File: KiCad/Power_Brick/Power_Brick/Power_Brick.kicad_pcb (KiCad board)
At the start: 2 copper layers, 70 x 70 mm, 109 parts, among them J1 Conn_01x10, J2 Conn_01x09, J3 MKDS5_2-9_5_1pos_PowerPad, J4 MKDS5_2-9_5_1pos_PowerPad, J5 MKDS5_2-9_5_4pos_PowerPad, J6 Conn_01x04, J7 Conn_01x04, Q1 CSD18540Q5B, Q2 CSD18540Q5B, Q3 CSD18540Q5B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

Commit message: KiCad beta
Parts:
- SW1: footprint PCM_SparkFun-Switch:Push_SMD_5.2x5.2mm_h1.9mm -> PCM_SparkFun-Switch:Push_SMD_4.6x2.8mm_h1.9mm
- moved D1 6.68 mm to (221.6, 126.5), turned to 180 degrees
- moved D2 6.58 mm to (203.0, 126.2), turned to 0 degrees
- moved D3 3.77 mm to (202.8, 132.0), turned to -90 degrees
- moved R1 3.45 mm to (219.6, 126.5)
- moved R2 3.45 mm to (218.4, 126.5)
- moved C1 1.93 mm to (205.0, 125.0)
- moved R3 1.89 mm to (206.0, 125.0)
- moved SW1 1.81 mm to (221.5, 129.0)
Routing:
- net GND: track 39.1 -> 31.3 mm, vias 139 -> 146
- net +3.3V: track 162.3 -> 158.3 mm
- net VBUS: track 36.4 -> 32.6 mm
- net Net-(D2-A): track 1.41 -> 5.19 mm
- net Net-(D1-A): track 3.96 -> 1.53 mm
- net /FAULT_N: track 28.9 -> 26.6 mm
- net +5V: track 12.3 -> 10.1 mm
- net /RESET: track 31.4 -> 30.2 mm

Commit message: KiCad beta
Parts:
- moved C8 31.6 mm to (186.2, 140.8), turned to 0 degrees
- moved NT8 2.00 mm to (190.5, 139.8)
- moved J5 0.59 mm to (212.5, 96.8)
- turned C6 to 0 degrees
- turned C7 to 0 degrees
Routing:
- net VBUS: track 32.6 -> 49.9 mm, vias 88 -> 97
- net GND: track 31.3 -> 24.7 mm, vias 146 -> 129

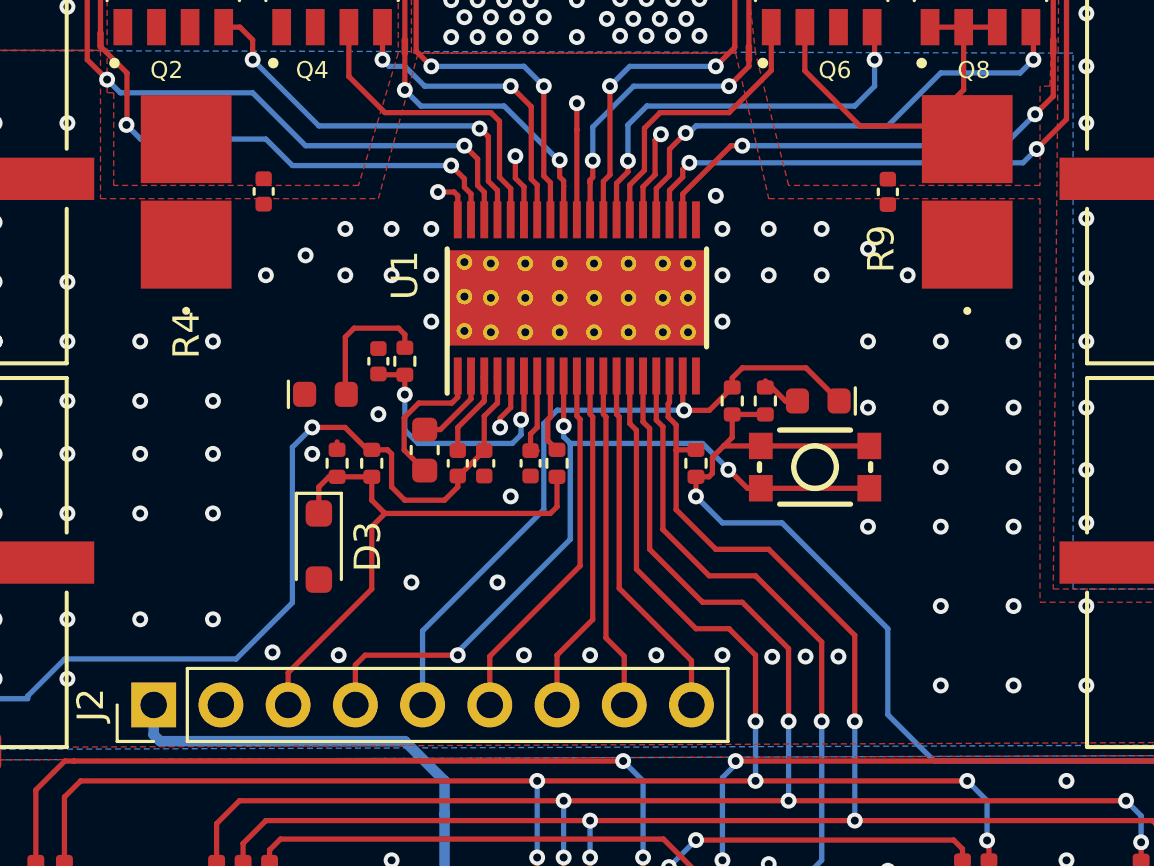
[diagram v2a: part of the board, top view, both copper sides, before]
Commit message: Revised fault and capacitor ratings
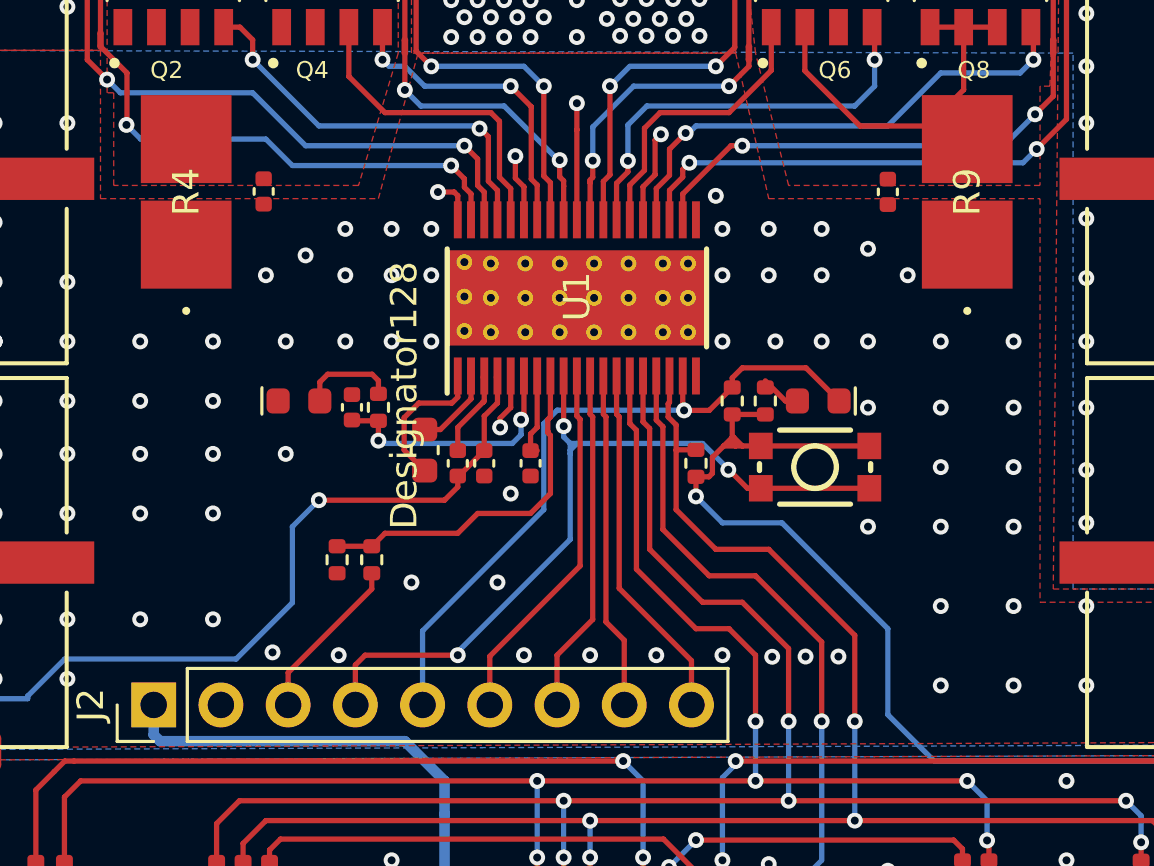
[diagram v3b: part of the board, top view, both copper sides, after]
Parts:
- removed D3: Zener, Diode_SMD:D_SOD-323_HandSoldering
- removed R5: 100k, PCM_SparkFun-Resistor:R_0402_1005Metric
- R7: value 22 -> 330
- moved R7 7.89 mm to (204.8, 132.5), turned to -90 degrees
- moved R6 3.64 mm to (203.4, 132.5), turned to 90 degrees
- moved C1 2.01 mm to (204.0, 126.7)
- moved R3 2.01 mm to (205.0, 126.7)
- moved D2 1.03 mm to (202.0, 126.5)
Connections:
- R6 pad 2: /SLEEP_N_IN -> /SLEEP_N
- R7 pad 1: /SLEEP_N_IN -> /SLEEP_N
- R7 pad 2: /SLEEP_N -> /SLEEP_N_IN
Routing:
- net /SLEEP_N_IN: track 21.2 -> 6.29 mm
- net /SLEEP_N: track 2.98 -> 13.4 mm
- net VBUS: track 49.9 -> 45.2 mm
- net Net-(D2-A): track 5.19 -> 3.65 mm
- net +3.3V: track 158.3 -> 159.2 mm
- net +5V: track 10.1 -> 9.60 mm
- net GND: track 24.7 -> 24.4 mm, vias 129 -> 133

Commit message: DRC, Silkscreen Updates
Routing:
- net GND: vias 133 -> 132
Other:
- board text added: "3.3"
- board text added: "A1"
- board text added: "A2"
- board text added: "B1"
- board text added: "B2"
- board text added: "CS0"
- board text added: "CS1"
- board text added: "CS2"
- board text added: "DR1"
- board text added: "DR2"
- board text added: "FLT"
- board text added: "GND"
- board text added: "RST"
- board text added: "SCL"
- board text added: "SDI"
- board text added: "SDO"
- board text added: "SLP"

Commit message: Digital Grount Updates
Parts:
- moved R6 4.62 mm to (208.0, 131.8)
- moved R7 4.32 mm to (209.0, 131.8)
- moved SW1 2.47 mm to (219.8, 130.8), turned to 90 degrees
- moved D2 1.25 mm to (203.0, 127.2), turned to 90 degrees
- moved D1 0.84 mm to (222.0, 127.2), turned to -90 degrees
- moved R1 0.62 mm to (219.2, 127.0)
- moved R2 0.51 mm to (218.2, 127.0)
- moved R8 0.27 mm to (217.2, 128.8), turned to 180 degrees
- moved R3 0.25 mm to (205.2, 126.8)
- moved C1 0.25 mm to (204.2, 126.7), turned to 90 degrees
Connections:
- J2 pad 2: GND -> GNDD
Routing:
- net /SLEEP_N: track 13.4 -> 8.47 mm
- net /SLEEP_N_IN: track 6.29 -> 11.2 mm
- net +3.3V: track 159.2 -> 154.5 mm
- net /FAULT_N: track 26.6 -> 23.6 mm
- net Net-(D1-A): track 1.53 -> 3.64 mm
- net +5V: track 9.60 -> 8.16 mm
- net VBUS: track 45.2 -> 44.5 mm
- net GND: track 24.4 -> 24.5 mm, vias 132 -> 138
- net GNDD: vias 29 -> 37
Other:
- board text added: "0"
- board text added: "1"
- board text added: "2"
- board text added: "G"

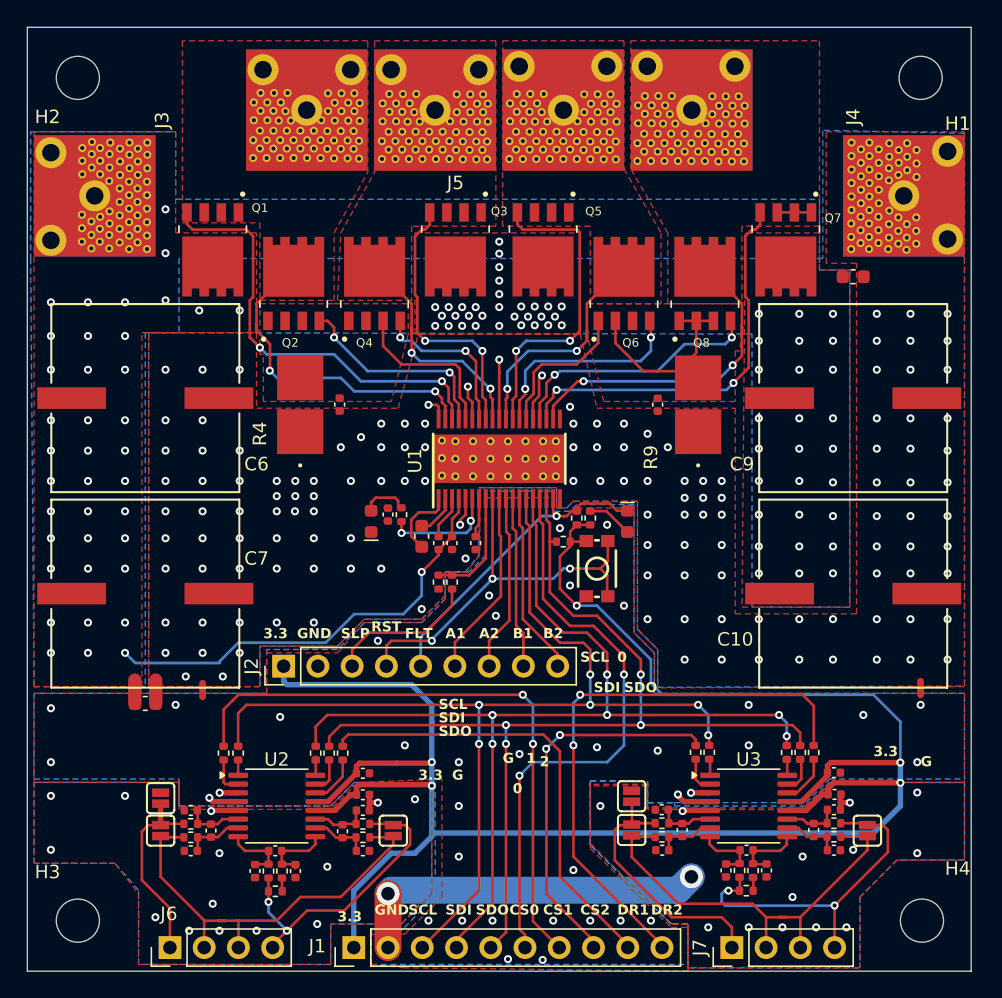
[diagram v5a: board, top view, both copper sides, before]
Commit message: 4 oz copper 0.3mm clearance
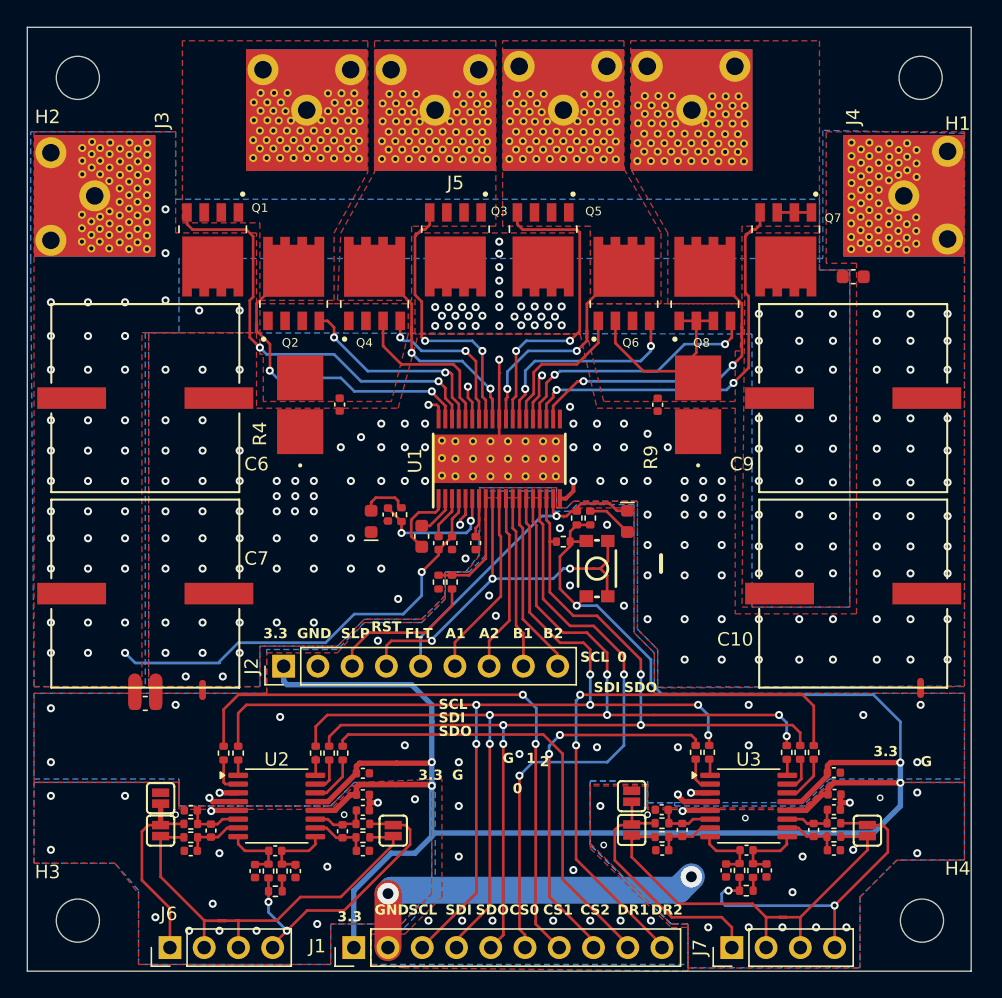
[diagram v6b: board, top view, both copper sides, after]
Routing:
- net GND: track 24.5 -> 29.4 mm
- net +5V: track 8.16 -> 9.80 mm
- net GNDA: track 30.9 -> 30.7 mm, vias 29 -> 35
- net GNDD: vias 37 -> 35
